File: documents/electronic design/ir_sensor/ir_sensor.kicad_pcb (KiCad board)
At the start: 2 copper layers, 11 parts, among them J1 Conn_01x06, J2 Conn_01x01, J3 Conn_01x06, J4 Conn_01x06, J5 Conn_01x06, J6 Conn_01x06, J7 Conn_01x06, U2 STM32F103HEADER, U3 MPU6050_module, U4 SE8R01_module

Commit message: adjust pcb
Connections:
- U2 pad 1: (no net) -> SE8R01_IRQ
- U2 pad 7: SE8R01_IRQ -> (no net)
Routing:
- net SE8R01_IRQ: track 18.2 -> 12.2 mm, vias 2 -> 0
- net +5V: track 75.2 -> 76.9 mm
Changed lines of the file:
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@@
     (links 56)
     (no_connects 0)
-    (area 0 0 0 0)
+    (area 17.39908 17.128741 81.05966 79.054773)
     (thickness 1.6)
     (drawings 0)
-    (tracks 227)
+    (tracks 214)
     (zones 0)
     (modules 11)
@@
     (fp_line (start 16.99 -1.75) (end 16.99 50.05) (layer F.CrtYd) (width 0.05))
     (fp_line (start 13.49 50.05) (end 16.99 50.05) (layer F.CrtYd) (width 0.05))
-    (pad 1 thru_hole rect (at 0 0) (size 2.032 1.7272) (drill 1.016) (layers *.Cu *.Mask F.SilkS))
+    (pad 1 thru_hole rect (at 0 0) (size 2.032 1.7272) (drill 1.016) (layers *.Cu *.Mask F.SilkS)
+      (net 12 SE8R01_IRQ))
     (pad 2 thru_hole oval (at 0 2.54) (size 2.032 1.7272) (drill 1.016) (layers *.Cu *.Mask F.SilkS)
       (net 11 SPI_SCK))
@@
     (pad 6 thru_hole oval (at 0 12.7) (size 2.032 1.7272) (drill 1.016) (layers *.Cu *.Mask F.SilkS)
       (net 3 SE8R01_CE))
-    (pad 7 thru_hole oval (at 0 15.24) (size 2.032 1.7272) (drill 1.016) (layers *.Cu *.Mask F.SilkS)
-      (net 12 SE8R01_IRQ))
+    (pad 7 thru_hole oval (at 0 15.24) (size 2.032 1.7272) (drill 1.016) (layers *.Cu *.Mask F.SilkS))
     (pad 8 thru_hole oval (at 0 17.78) (size 2.032 1.7272) (drill 1.016) (layers *.Cu *.Mask F.SilkS))
     (pad 9 thru_hole oval (at 0 20.32) (size 2.032 1.7272) (drill 1.016) (layers *.Cu *.Mask F.SilkS))
@@
   (segment (start 43.390418 37.667342) (end 45.420578 37.667342) (width 0.6) (layer F.Cu) (net 4))
   (segment (start 45.420578 37.667342) (end 45.99122 37.0967) (width 0.6) (layer F.Cu) (net 4))
-  (segment (start 42.36268 24.35098) (end 43.640581 23.073079) (width 0.6) (layer F.Cu) (net 5))
-  (segment (start 40.89908 24.35098) (end 42.36268 24.35098) (width 0.6) (layer F.Cu) (net 5))
-  (segment (start 43.640581 23.073079) (end 52.802609 23.073079) (width 0.6) (layer F.Cu) (net 5))
+  (segment (start 59.931197 38.466827) (end 59.931197 49.573077) (width 0.6) (layer F.Cu) (net 5))
+  (segment (start 57.614629 36.150259) (end 59.931197 38.466827) (width 0.6) (layer F.Cu) (net 5))
   (segment (start 52.802609 23.073079) (end 57.614629 27.885099) (width 0.6) (layer F.Cu) (net 5))
+  (segment (start 62.69482 52.3367) (end 62.84722 52.3367) (width 0.6) (layer F.Cu) (net 5))
+  (segment (start 42.176981 23.073079) (end 52.802609 23.073079) (width 0.6) (layer F.Cu) (net 5))
+  (segment (start 40.89908 24.35098) (end 42.176981 23.073079) (width 0.6) (layer F.Cu) (net 5))
   (segment (start 57.614629 27.885099) (end 57.614629 36.150259) (width 0.6) (layer F.Cu) (net 5))
-  (segment (start 57.614629 36.150259) (end 59.931197 38.466827) (width 0.6) (layer F.Cu) (net 5))
-  (segment (start 59.931197 38.466827) (end 59.931197 49.573077) (width 0.6) (layer F.Cu) (net 5))
   (segment (start 59.931197 49.573077) (end 62.69482 52.3367) (width 0.6) (layer F.Cu) (net 5))
-  (segment (start 62.69482 52.3367) (end 62.84722 52.3367) (width 0.6) (layer F.Cu) (net 5))
-  (segment (start 41.588169 26.16699) (end 41.625069 26.13009) (width 0.6) (layer F.Cu) (net 6))
-  (segment (start 44.98349 24.17309) (end 52.34697 24.17309) (width 0.6) (layer F.Cu) (net 6))
-  (segment (start 43.02649 26.13009) (end 44.98349 24.17309) (width 0.6) (layer F.Cu) (net 6))
-  (segment (start 58.831188 51.013068) (end 62.69482 54.8767) (width 0.6) (layer F.Cu) (net 6))
-  (segment (start 62.69482 54.8767) (end 62.84722 54.8767) (width 0.6) (layer F.Cu) (net 6))
-  (segment (start 52.34697 24.17309) (end 56.514618 28.340738) (width 0.6) (layer F.Cu) (net 6))
-  (segment (start 40.02269 26.16699) (end 41.588169 26.16699) (width 0.6) (layer F.Cu) (net 6))
-  (segment (start 38.35908 24.35098) (end 38.35908 24.50338) (width 0.6) (layer F.Cu) (net 6))
-  (segment (start 38.35908 24.50338) (end 40.02269 26.16699) (width 0.6) (layer F.Cu) (net 6))
-  (segment (start 41.625069 26.13009) (end 43.02649 26.13009) (width 0.6) (layer F.Cu) (net 6))
-  (segment (start 56.514618 28.340738) (end 56.514619 36.605899) (width 0.6) (layer F.Cu) (net 6))
-  (segment (start 56.514619 36.605899) (end 58.831186 38.922466) (width 0.6) (layer F.Cu) (net 6))
-  (segment (start 58.831186 38.922466) (end 58.831188 51.013068) (width 0.6) (layer F.Cu) (net 6))
+  (segment (start 38.35908 24.50338) (end 38.35908 24.35098) (width 0.6) (layer F.Cu) (net 6))
+  (segment (start 43.582069 24.17309) (end 41.48667 26.268489) (width 0.6) (layer F.Cu) (net 6))
+  (segment (start 52.34697 24.17309) (end 43.582069 24.17309) (width 0.6) (layer F.Cu) (net 6))
+  (segment (start 56.514618 28.340738) (end 52.34697 24.17309) (width 0.6) (layer F.Cu) (net 6))
+  (segment (start 41.48667 26.268489) (end 40.124189 26.268489) (width 0.6) (layer F.Cu) (net 6))
+  (segment (start 58.831186 38.922466) (end 56.514619 36.605899) (width 0.6) (layer F.Cu) (net 6))
+  (segment (start 58.831188 51.013068) (end 58.831186 38.922466) (width 0.6) (layer F.Cu) (net 6))
+  (segment (start 40.124189 26.268489) (end 38.35908 24.50338) (width 0.6) (layer F.Cu) (net 6))
+  (segment (start 62.69482 54.8767) (end 58.831188 51.013068) (width 0.6) (layer F.Cu) (net 6))
+  (segment (start 62.84722 54.8767) (end 62.69482 54.8767) (width 0.6) (layer F.Cu) (net 6))
+  (segment (start 56.514619 36.605899) (end 56.514618 28.340738) (width 0.6) (layer F.Cu) (net 6))
   (segment (start 28.19908 22.73498) (end 28.19908 24.35098) (width 0.6) (layer F.Cu) (net 7))
   (segment (start 62.242762 20.873058) (end 30.061002 20.873058) (width 0.6) (layer F.Cu) (net 7))
@@
   (segment (start 47.38624 29.69768) (end 47.60722 29.4767) (width 0.6) (layer F.Cu) (net 11))
   (via (at 44.3865 29.69768) (size 2) (drill 0.7) (layers F.Cu B.Cu) (net 11))
-  (segment (start 43.948961 41.035379) (end 41.806201 38.892619) (width 0.6) (layer B.Cu) (net 12))
-  (segment (start 41.806201 32.887834) (end 41.806201 31.473621) (width 0.6) (layer B.Cu) (net 12))
-  (via (at 41.806201 31.473621) (size 2) (drill 0.7) (layers F.Cu B.Cu) (net 12))
-  (segment (start 41.407902 31.87192) (end 41.806201 31.473621) (width 0.6) (layer F.Cu) (net 12))
-  (segment (start 41.806201 38.892619) (end 41.806201 32.887834) (width 0.6) (layer B.Cu) (net 12))
-  (segment (start 38.5191 31.87192) (end 41.407902 31.87192) (width 0.6) (layer F.Cu) (net 12))
-  (segment (start 45.090282 42.1767) (end 44.94896 42.035378) (width 0.6) (layer F.Cu) (net 12))
-  (via (at 43.948961 41.035379) (size 2) (drill 0.7) (layers F.Cu B.Cu) (net 12))
-  (segment (start 47.60722 42.1767) (end 45.090282 42.1767) (width 0.6) (layer F.Cu) (net 12))
-  (segment (start 44.94896 42.035378) (end 43.948961 41.035379) (width 0.6) (layer F.Cu) (net 12))
-  (segment (start 47.58182 42.2021) (end 47.60722 42.1767) (width 0.6) (layer F.Cu) (net 12))
-  (segment (start 47.45482 42.1767) (end 47.60722 42.1767) (width 0.6) (layer F.Cu) (net 12))
+  (segment (start 42.21734 28.82138) (end 42.21734 30.63748) (width 0.6) (layer F.Cu) (net 12))
+  (segment (start 42.21734 30.63748) (end 40.9829 31.87192) (width 0.6) (layer F.Cu) (net 12))
+  (segment (start 44.10202 26.9367) (end 42.21734 28.82138) (width 0.6) (layer F.Cu) (net 12))
+  (segment (start 47.60722 26.9367) (end 44.10202 26.9367) (width 0.6) (layer F.Cu) (net 12))
+  (segment (start 38.5191 31.87192) (end 40.9829 31.87192) (width 0.6) (layer F.Cu) (net 12))
   (segment (start 47.60722 70.1167) (end 47.75962 70.1167) (width 0.6) (layer F.Cu) (net 13))
   (segment (start 47.75962 70.1167) (end 50.90922 66.9671) (width 0.6) (layer F.Cu) (net 13))
+  (segment (start 41.942309 27.3685) (end 23.6347 27.3685) (width 0.6) (layer F.Cu) (net 13))
+  (segment (start 50.90922 66.9671) (end 50.90922 26.919098) (width 0.6) (layer F.Cu) (net 13))
+  (segment (start 50.90922 26.919098) (end 49.263221 25.273099) (width 0.6) (layer F.Cu) (net 13))
+  (segment (start 49.263221 25.273099) (end 44.03771 25.273099) (width 0.6) (layer F.Cu) (net 13))
+  (segment (start 44.03771 25.273099) (end 41.942309 27.3685) (width 0.6) (layer F.Cu) (net 13))
+  (segment (start 23.6347 27.3685) (end 23.11908 26.85288) (width 0.6) (layer F.Cu) (net 13))
+  (segment (start 23.11908 26.85288) (end 23.11908 24.35098) (width 0.6) (layer F.Cu) (net 13))
   (segment (start 23.11908 24.50338) (end 23.11908 24.35098) (width 0.6) (layer F.Cu) (net 13))
-  (segment (start 42.080708 27.230101) (end 42.043808 27.267001) (width 0.6) (layer F.Cu) (net 13))
-  (segment (start 50.90922 26.919098) (end 49.263221 25.273099) (width 0.6) (layer F.Cu) (net 13))
-  (segment (start 43.677709 27.230101) (end 42.080708 27.230101) (width 0.6) (layer F.Cu) (net 13))
-  (segment (start 45.634711 25.273099) (end 43.677709 27.230101) (width 0.6) (layer F.Cu) (net 13))
-  (segment (start 42.043808 27.267001) (end 39.455291 27.267001) (width 0.6) (layer F.Cu) (net 13))
-  (segment (start 49.263221 25.273099) (end 45.634711 25.273099) (width 0.6) (layer F.Cu) (net 13))
-  (segment (start 50.90922 66.9671) (end 50.90922 26.919098) (width 0.6) (layer F.Cu) (net 13))
-  (segment (start 25.54986 26.93416) (end 23.11908 24.50338) (width 0.6) (layer F.Cu) (net 13))
-  (segment (start 39.12245 26.93416) (end 25.54986 26.93416) (width 0.6) (layer F.Cu) (net 13))
-  (segment (start 39.455291 27.267001) (end 39.12245 26.93416) (width 0.6) (layer F.Cu) (net 13))
   (segment (start 42.39006 51.79822) (end 44.39158 49.7967) (width 0.6) (layer F.Cu) (net 14))
   (segment (start 44.39158 49.7967) (end 47.60722 49.7967) (width 0.6) (layer F.Cu) (net 14))

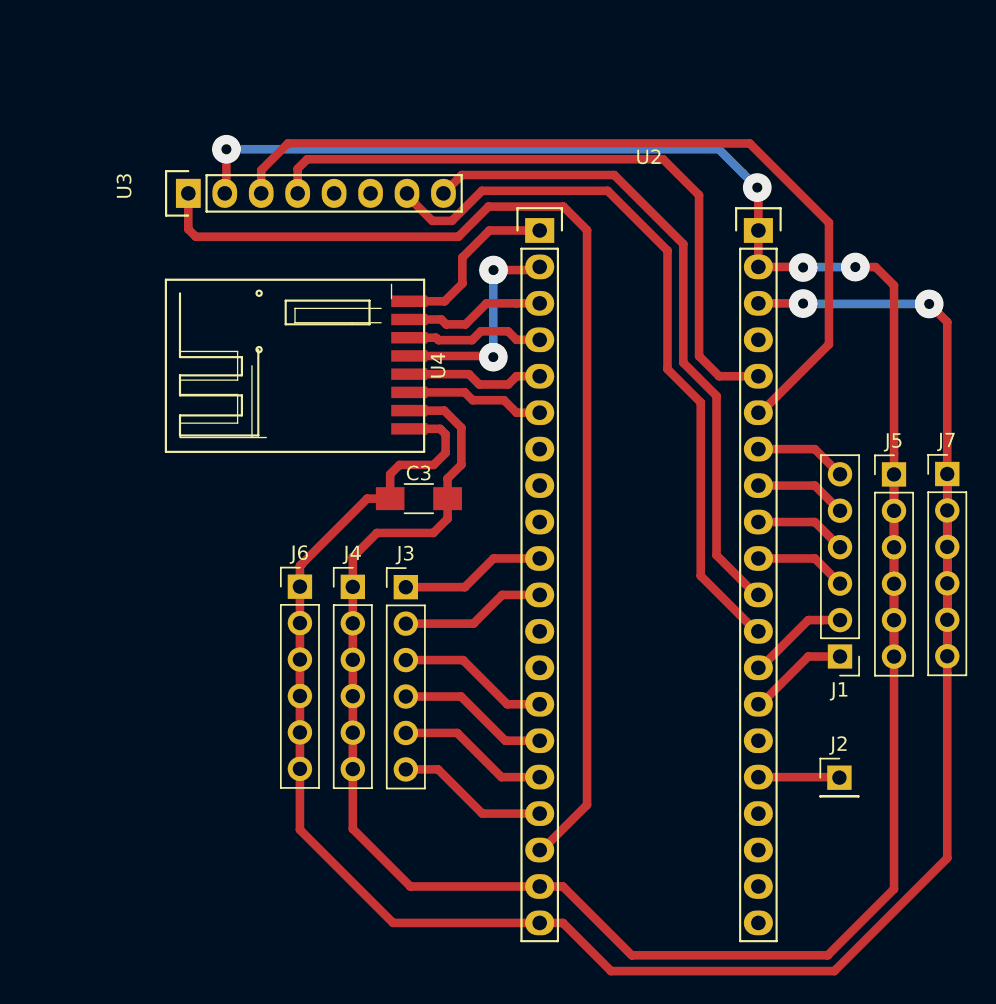
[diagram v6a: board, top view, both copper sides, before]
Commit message: adjust pcb, pin assignments
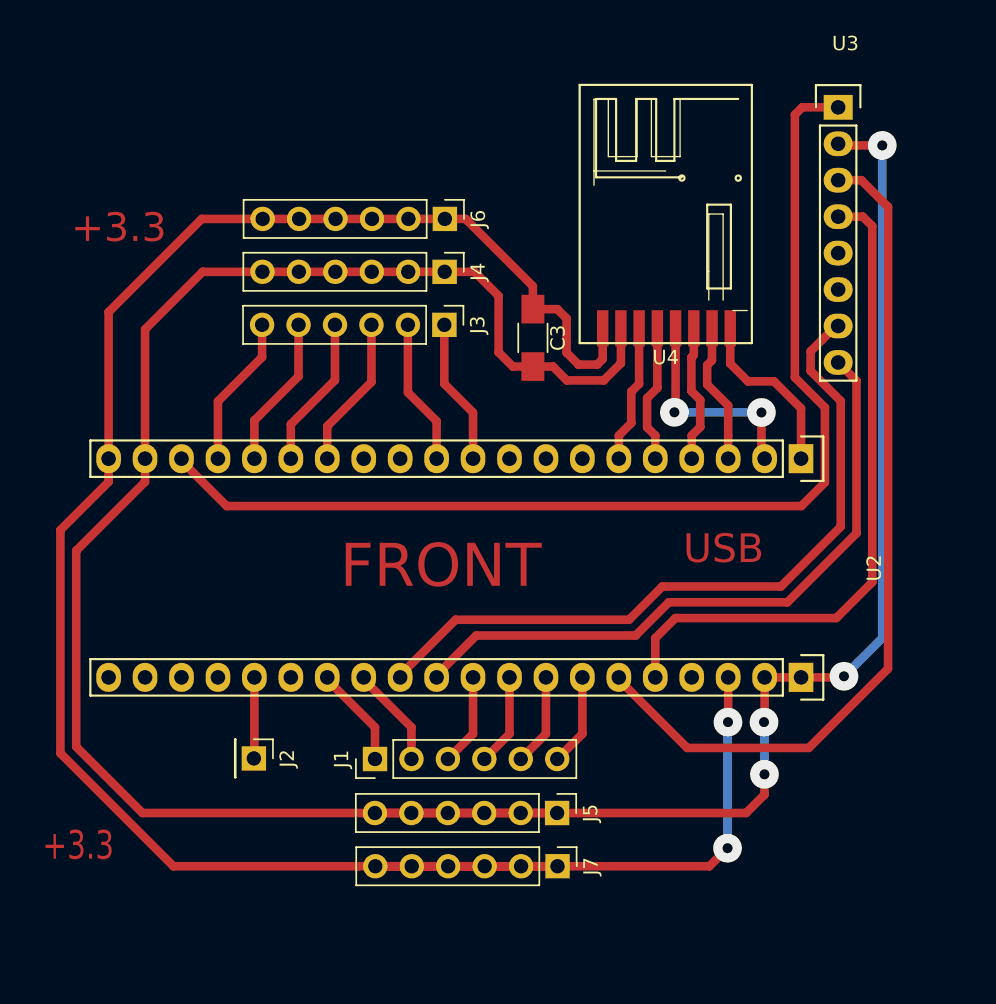
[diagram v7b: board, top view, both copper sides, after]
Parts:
- moved U3 45.7 mm to (68.4, 18.4), turned to 0 degrees
- moved J2 40.8 mm to (27.7, 63.7), turned to 270 degrees
- moved J7 38.5 mm to (48.9, 71.2), turned to 270 degrees
- moved J5 33.3 mm to (48.8, 67.5), turned to 270 degrees
- moved J1 33.2 mm to (36.1, 63.8), turned to 90 degrees
- moved J6 27.5 mm to (41.0, 26.1), turned to 270 degrees
- moved U2 24.2 mm to (65.8, 42.8), turned to 270 degrees
- moved J4 22.9 mm to (41.0, 29.8), turned to 270 degrees
- moved J3 18.5 mm to (41.0, 33.5), turned to 270 degrees
- moved C3 13.7 mm to (47.1, 34.4), turned to 270 degrees
- moved U4 13.2 mm to (50.4, 34.8), turned to 0 degrees
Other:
- board text added: "+3.3"
- board text added: "FRONT"
- board text added: "USB"
